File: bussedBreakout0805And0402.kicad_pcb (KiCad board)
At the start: 2 copper layers, 2.9 x 2.9 mm, 46 parts, among them J1 Conn_01x12_Pin, J10 Conn_01x06_Pin, J11 Conn_01x06_Pin, J12 Conn_01x06_Pin, J13 Conn_01x06_Pin, J14 Conn_01x06_Pin, J15 Conn_01x06_Pin, J16 Conn_01x06_Pin, J17 Conn_01x06_Pin, J18 Conn_01x06_Pin, J19 Conn_01x06_Pin, J2 Conn_01x01_Pin, J20 Conn_01x06_Pin, J21 Conn_01x06_Pin, J22 Conn_01x06_Pin, J23 Conn_01x06_Pin, J24 Conn_01x06_Pin, J25 Conn_01x06_Pin, J26 Conn_01x06_Pin, J27 Conn_01x06_Pin, J28 Conn_01x06_Pin, J29 Conn_01x06_Pin, J3 Conn_01x01_Pin, J30 Conn_01x06_Pin, J31 Conn_01x06_Pin, J32 Conn_01x06_Pin, J4 Conn_01x05_Pin, J5 Conn_01x05_Pin, J6 Conn_01x01_Pin, J7 Conn_01x01_Pin, J8 Conn_01x12_Pin, J9 Conn_01x06_Pin

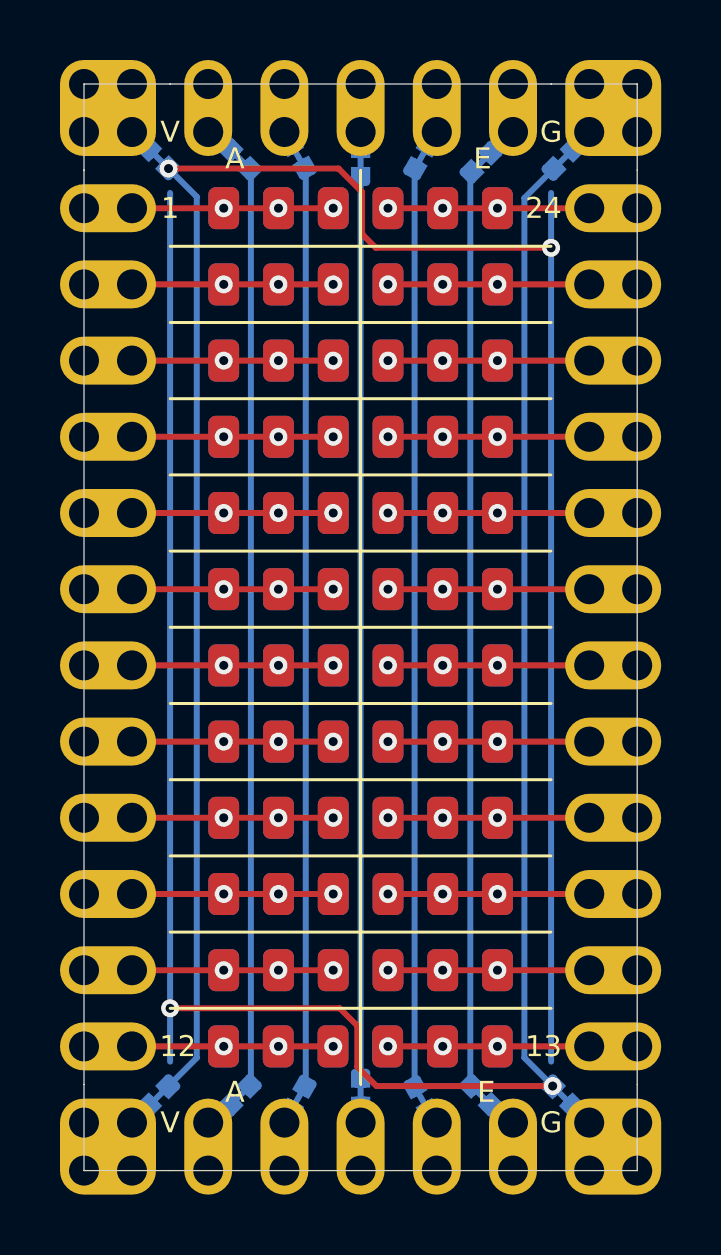
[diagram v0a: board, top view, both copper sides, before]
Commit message: Replace 1/3 of top 0805 footprints with twice as many 0402 ones
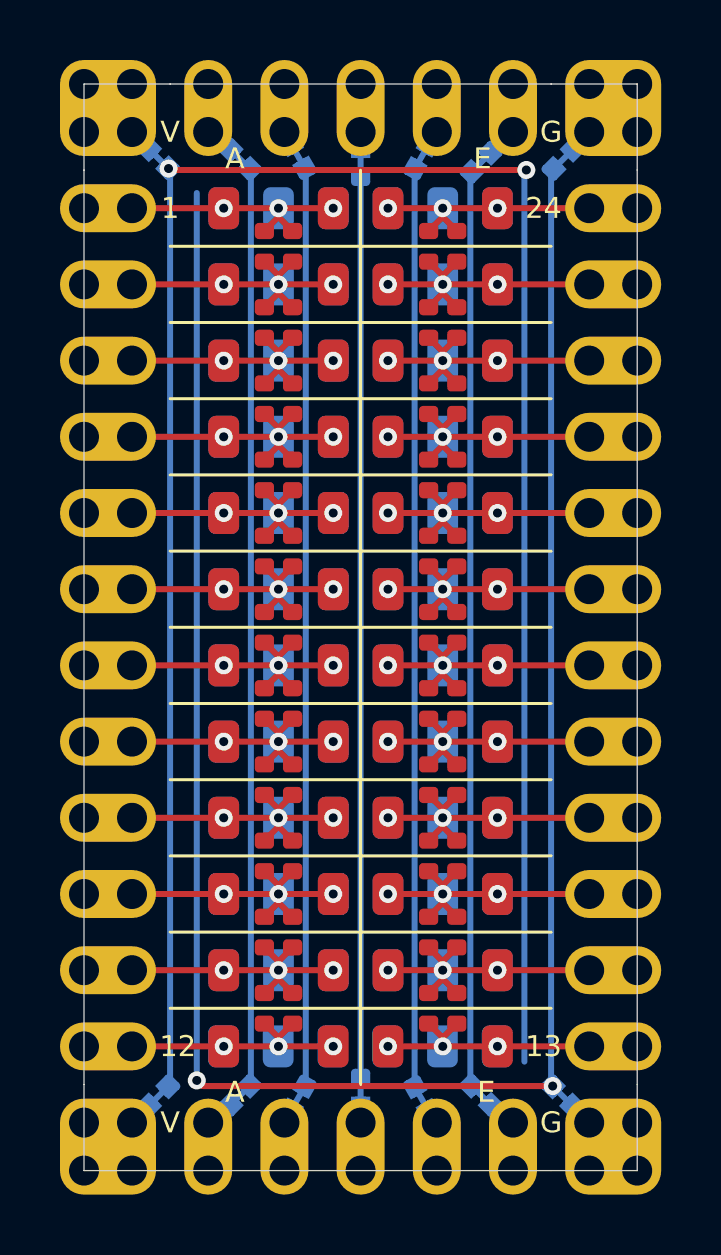
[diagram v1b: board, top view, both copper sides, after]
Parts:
- J21, J32: value Conn_01x06_Pin -> Conn_01x12_Pin; footprint SMD:SMD_0805_grid_1x6 -> SMD:SMD_0805_grid_1x6_interleaved_0402_1x2
- J22, J23, J24, J25, J26, J27, J28, J29, J30, J31: value Conn_01x06_Pin -> Conn_01x20_Pin; footprint SMD:SMD_0805_grid_1x6 -> SMD:SMD_0805_grid_1x6_interleaved_0402_2x2
- turned J21 to 180 degrees
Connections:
- J21 pad 1: /1 -> /24
- J21 pad 2: /1 -> /24
- J21 pad 3: /1 -> /24
- J21 pad 5: /24 -> /1
- J21 pad 6: /24 -> /1
- J22 pad 4: /23 -> /2
- J22 pad 5: /23 -> /2
- J22 pad 6: /23 -> /2
- J23 pad 4: /22 -> /3
- J23 pad 5: /22 -> /3
- J23 pad 6: /22 -> /3
- J24 pad 4: /21 -> /4
- J24 pad 5: /21 -> /4
- J24 pad 6: /21 -> /4
- J25 pad 4: /20 -> /5
- J25 pad 5: /20 -> /5
- J25 pad 6: /20 -> /5
- J26 pad 4: /19 -> /6
- J26 pad 5: /19 -> /6
- J26 pad 6: /19 -> /6
- J27 pad 4: /18 -> /7
- J27 pad 5: /18 -> /7
- J27 pad 6: /18 -> /7
- J28 pad 4: /17 -> /8
- J28 pad 5: /17 -> /8
- J28 pad 6: /17 -> /8
- J29 pad 4: /16 -> /9
- J29 pad 5: /16 -> /9
- J29 pad 6: /16 -> /9
- J30 pad 4: /15 -> /10
- J30 pad 5: /15 -> /10
- J30 pad 6: /15 -> /10
- J31 pad 4: /14 -> /11
- J31 pad 5: /14 -> /11
- J31 pad 6: /14 -> /11
- J32 pad 4: /13 -> /12
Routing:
- net /23: track 6.71 -> 10.1 mm
- net /9: track 6.71 -> 9.95 mm
- net /4: track 6.71 -> 9.95 mm
- net /3: track 6.71 -> 9.95 mm
- net /11: track 6.71 -> 9.95 mm
- net /10: track 6.71 -> 9.95 mm
- net /16: track 6.71 -> 9.95 mm
- net /21: track 6.71 -> 9.95 mm
- net /2: track 6.71 -> 9.95 mm
- net /22: track 6.71 -> 9.95 mm
- net /15: track 6.71 -> 9.95 mm
- net /8: track 6.71 -> 9.95 mm
- net /7: track 6.71 -> 9.95 mm
- net /6: track 6.71 -> 9.95 mm
- net /5: track 6.71 -> 9.95 mm
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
